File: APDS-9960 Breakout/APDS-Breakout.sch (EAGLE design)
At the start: 25 parts, among them Q1 BSS138, Q2 BSS138, Q3 BSS138, U1 APDS-9960

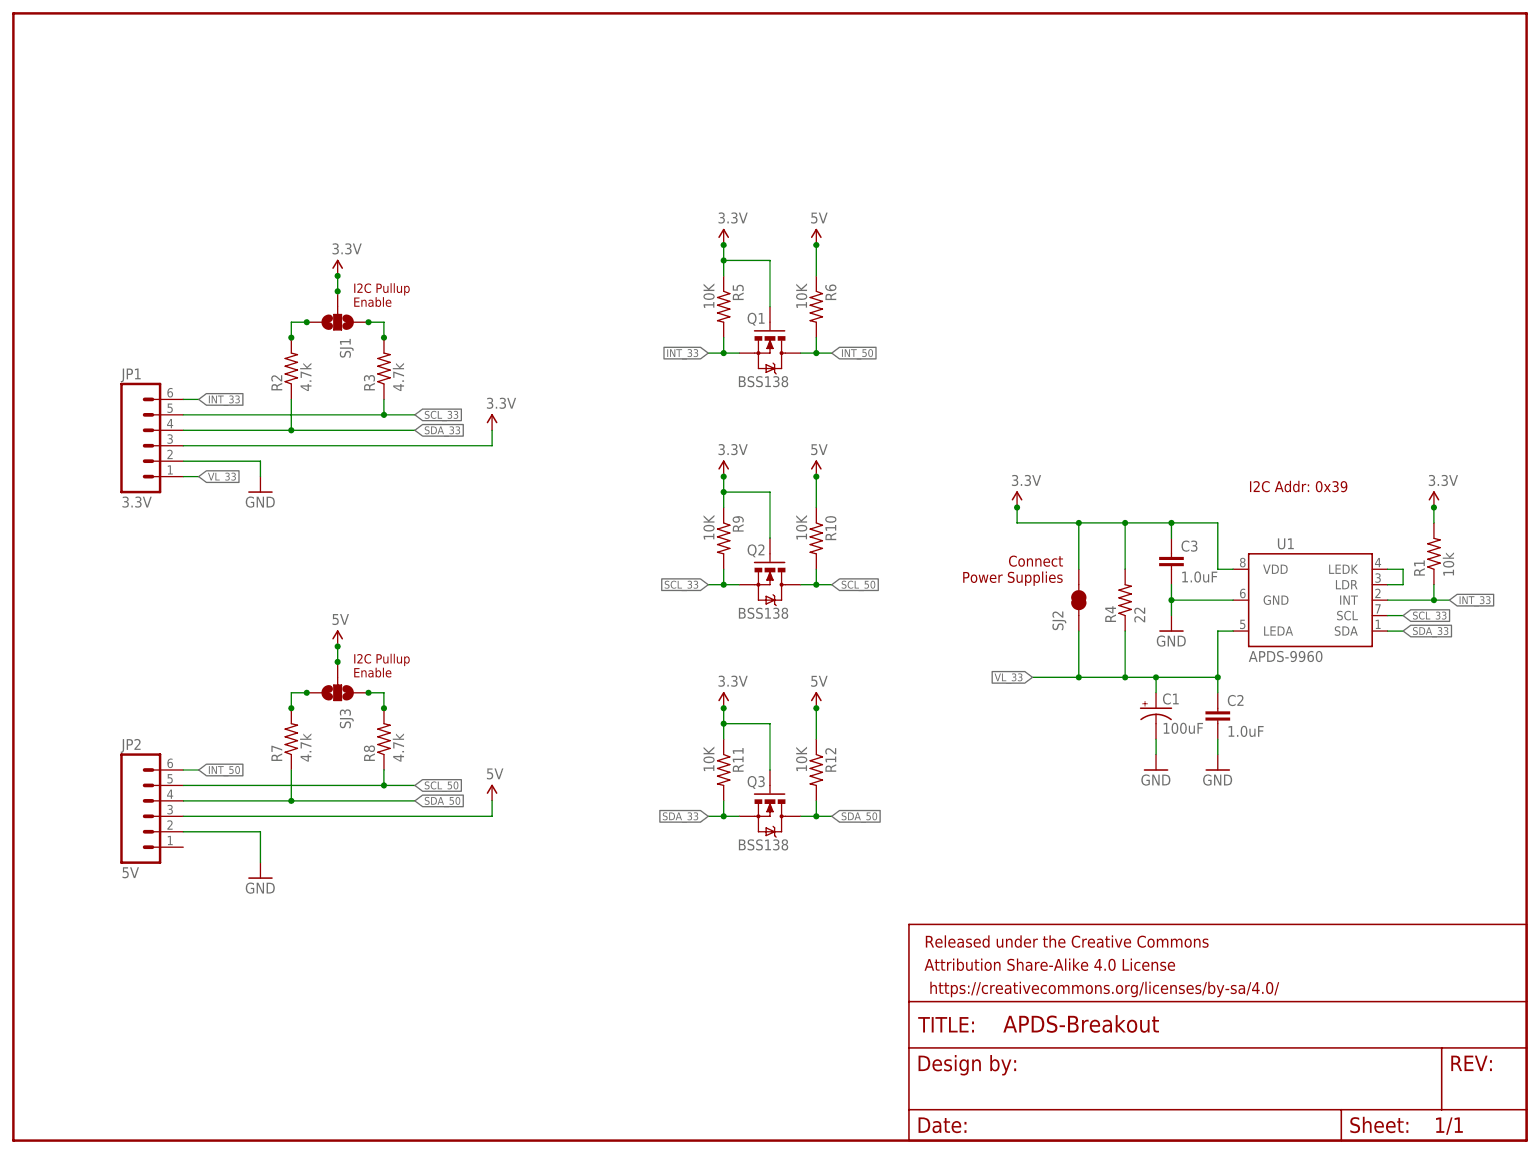
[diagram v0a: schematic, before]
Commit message: Initial Design Complete
Modifications to the SparkFun design (most significant to least):
1) Rotate and relocate sensor as close as possible to edge of board.
Reason: I want to be able to put this sensor board into an enclosure
next to an LCD. The sensor needs to be as close to the LCD for both to
fit in the window.

2) Add location on back of board for large electrolytic capacitor.
Reason: placing the capacitor behind the sensor improves packaging
options for the board and sensor.

3) Added voltage regulator and level shifting components to make the
board 5V safe.
Reason: Easier to integrate with Arduinos and other 5V micros.
Note: In my understanding of the APDS datasheet the sensor can pull up
to 790mA. Because of this, a 1A regulator was selected, MCP1826T. Device
and footprint created in my Eagle library
(https://github.com/akreager/ATK_Engineering-Eagle_Library). I2C level
shifter design "borrowed" from SparkFun login level shifter board.

4) (Least important) Attempted to add provisions to be able to break
board into two pieces and reconnet with jumper wires.
Reason: Packaging.
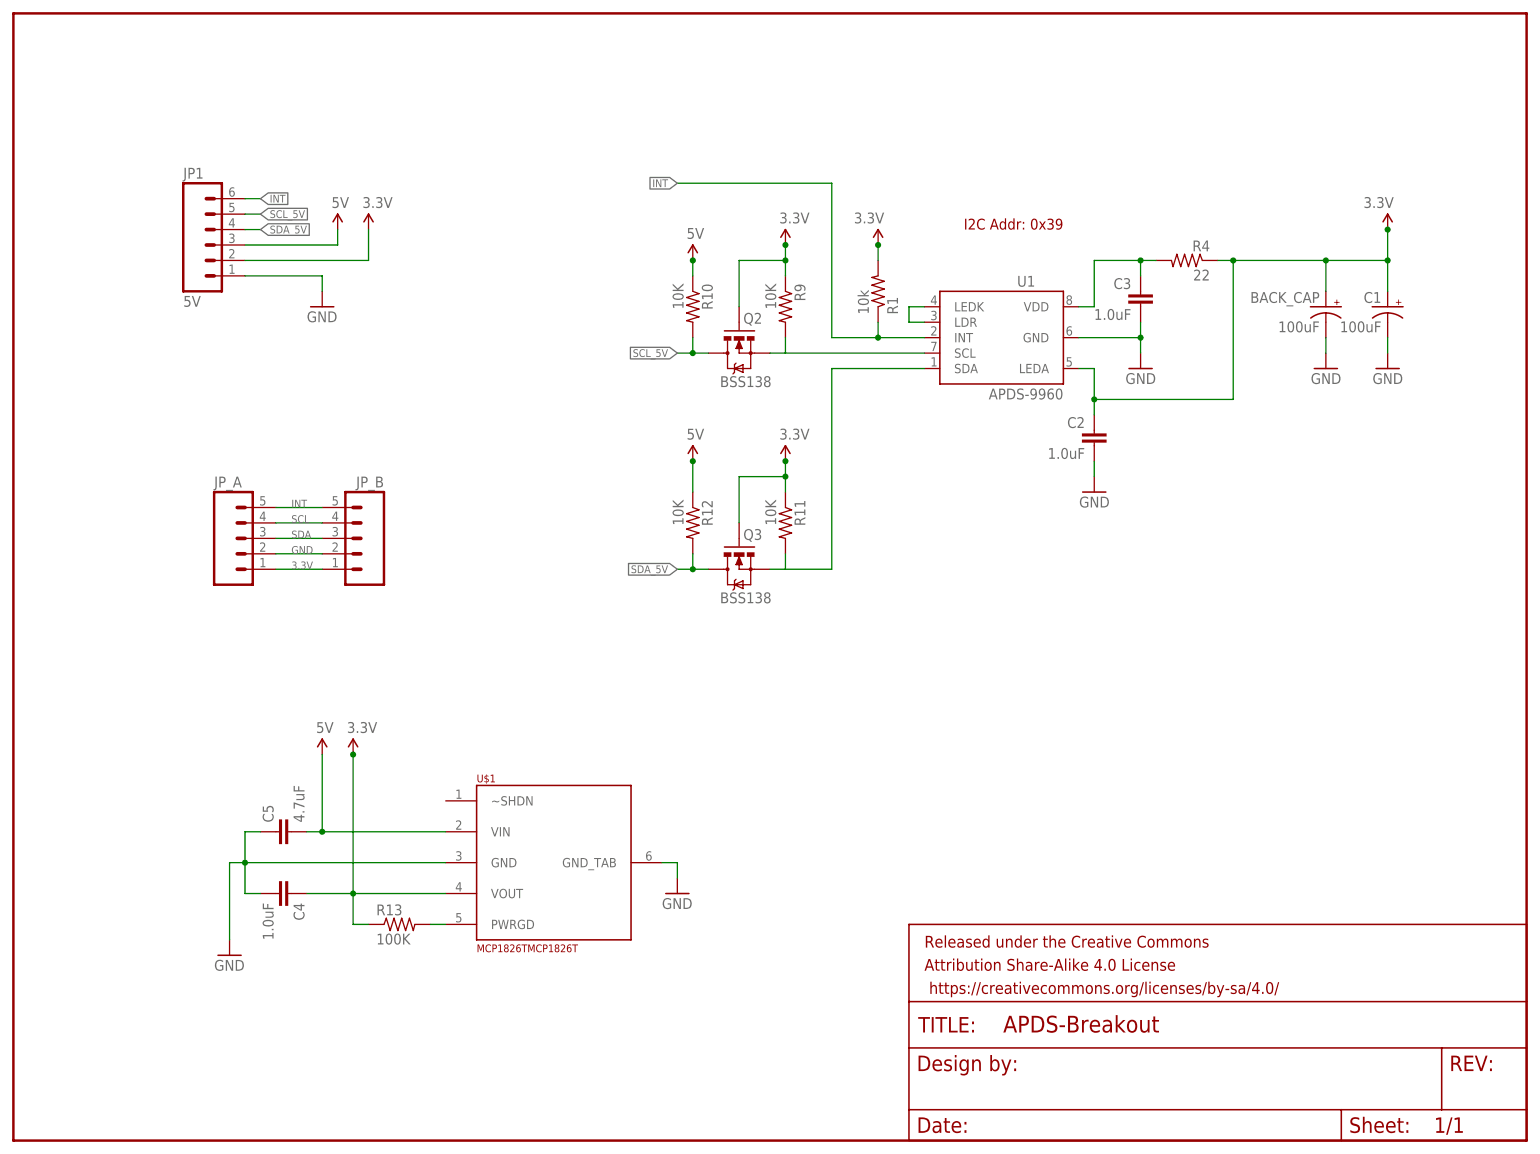
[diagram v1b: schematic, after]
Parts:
- removed JP2: 5V, SparkFun-Connectors:M06NO_SILK_FEMALE_PTH
- removed Q1: BSS138, SparkFun:MOSFET-NCHANNELSMD
- removed R2, R3, R7, R8: 4.7k, SparkFun-Resistors:4.7KOHM1/10W1%(0603)
- removed R5, R6: 10K, SparkFun:RESISTOR0603-RES
- removed SJ1, SJ3: (no value), SparkFun-Passives:SOLDERJUMPER_2WAYPASTE1&2&3
- removed SJ2: SOLDERJUMPERNC, SparkFun-Retired:SOLDERJUMPERNC
- added BACK_CAP: 100uF, SparkFun-Capacitors:100UF-10V-10%(TANT)
- added C4: 1.0uF, SparkFun-Capacitors:1.0UF-16V-10%(0603)
- added C5: 4.7uF, SparkFun-Capacitors:1.0UF-16V-10%(0603)
- added JP_A, JP_B: (no value), SparkFun-Connectors:M05PTH
- added R13: 100K, SparkFun:RESISTOR0603-RES
- added U$1: MCP1826TMCP1826T, ATK_lib:MCP1826TMCP1826T
- JP1: value 3.3V -> 5V
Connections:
- removed net INT_33: JP1.6, Q1.S, R1.1, R5.2, U1.INT
- removed net INT_50: JP2.6, Q1.D, R6.2
- removed net N$2: R3.2, SJ1.1
- removed net N$3: R7.2, SJ3.3
- removed net N$5: R8.2, SJ3.1
- removed net SCL_33: JP1.5, Q2.S, R3.1, R9.2, U1.SCL
- removed net SCL_50: JP2.5, Q2.D, R10.2, R8.1
- removed net SDA_33: JP1.4, Q3.S, R11.2, R2.1, U1.SDA
- removed net SDA_50: JP2.4, Q3.D, R12.2, R7.1
- removed net VL_33: C1.+, C2.1, JP1.1, R4.1, SJ2.1, U1.LEDA
- new net INT: JP1.6, JP_A.5, JP_B.5, R1.1, U1.INT
- new net N$6: R13.2, U$1.PWRGD
- new net SCL: JP_A.4, JP_B.4, Q2.S, R9.2, U1.SCL
- new net SCL_5V: JP1.5, Q2.D, R10.2
- new net SDA: JP_A.3, JP_B.3, Q3.S, R11.2, U1.SDA
- new net SDA_5V: JP1.4, Q3.D, R12.2
- net 3.3V: now also BACK_CAP.+, C1.+, C2.1, C4.1, JP1.2, JP_A.1, JP_B.1, R13.1, R4.1, U$1.VOUT, U1.LEDA; no longer C3.1, JP1.3, Q1.G, R4.2, R5.1, SJ1.2, SJ2.2, U1.VDD
- net 5V: now also C5.2, JP1.3, U$1.VIN; no longer JP2.3, R6.1, SJ3.2
- net GND: now also BACK_CAP.-, C4.2, C5.1, JP1.1, JP_A.2, JP_B.2, U$1.GND, U$1.GND_TAB; no longer JP1.2, JP2.2
- net N$1: now also C3.1, R4.2, U1.VDD; no longer R2.2, SJ1.3
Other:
- note removed: "Connect Power Supplies"
- note removed: "I2C Pullup Enable"
- moved on the sheet: C1, C2, C3, JP1, Q2, Q3, R1, R10, R11, R12, R4, R9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
